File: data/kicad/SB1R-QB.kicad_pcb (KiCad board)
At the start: 4 copper layers, 230 x 228 mm, 5 parts

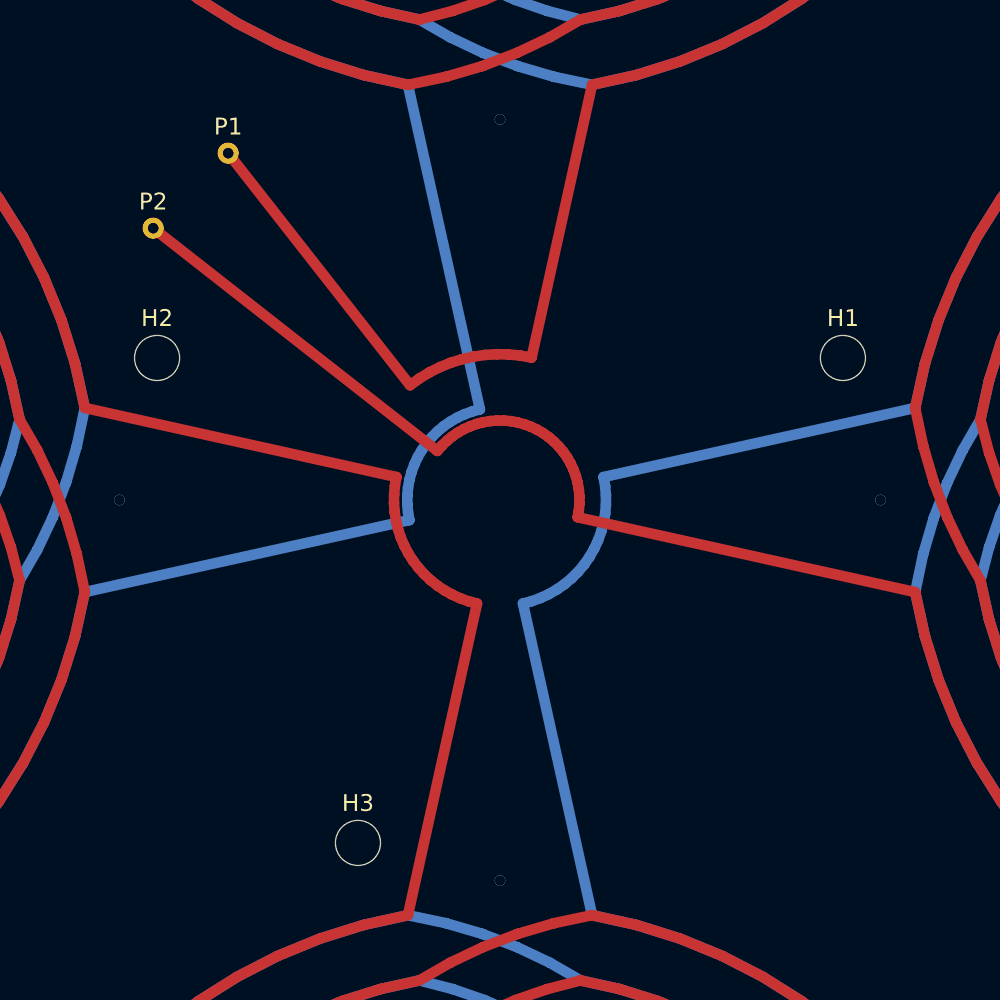
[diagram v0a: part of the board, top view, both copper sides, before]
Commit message: Damping resistors 680 ohm, results, docs and regression for SB1R-Q
- RD1/RD2 value 680 ohm (minimax first gate over Cself 50-200 pF with the
  real AB1T input): 5.1-5.5 us aligned, 7.1-7.5 us at the worst real leak
  (10 mV); gated noise +4 % at 6 us, < 2 % from 20 us. Firmware rule: keep
  BLANK open through turn-off unless the leak exceeds amplifier headroom.
- QB leak after moving its terminals to r23 and re-tuning B (9/9/9/20/6):
  0.07 / 0.59 / 6.0 / 10.3 mV (was 0.005 / 0.85 / 4.4 / 11.0 mV).
- Regenerated SB1R-QA/QB Gerbers and KiCad files, seeds and results;
  sbq_damping.json replaced by sbq_damping2.json; figures SBQ_DAMPING2,
  RX_PLATFORM_QUAD and LEVELS_SCHEMATIC redrawn.
- DESIGN_STATE, CORRECTIONS (5 rows), ASSUMPTIONS (row 14, new row 21),
  OPEN_ITEMS (1 and 12), check counts, stale P01/P02/C04 prompts.
- regress.py: 47 geometry checks, damping fitted, first gate and noise.

Co-Authored-By: Claude Opus 5.5 <noreply@anthropic.com>
Claude-Session: https://claude.ai/code/session_01SK9nuqTzvCJwnmscD6XRZs
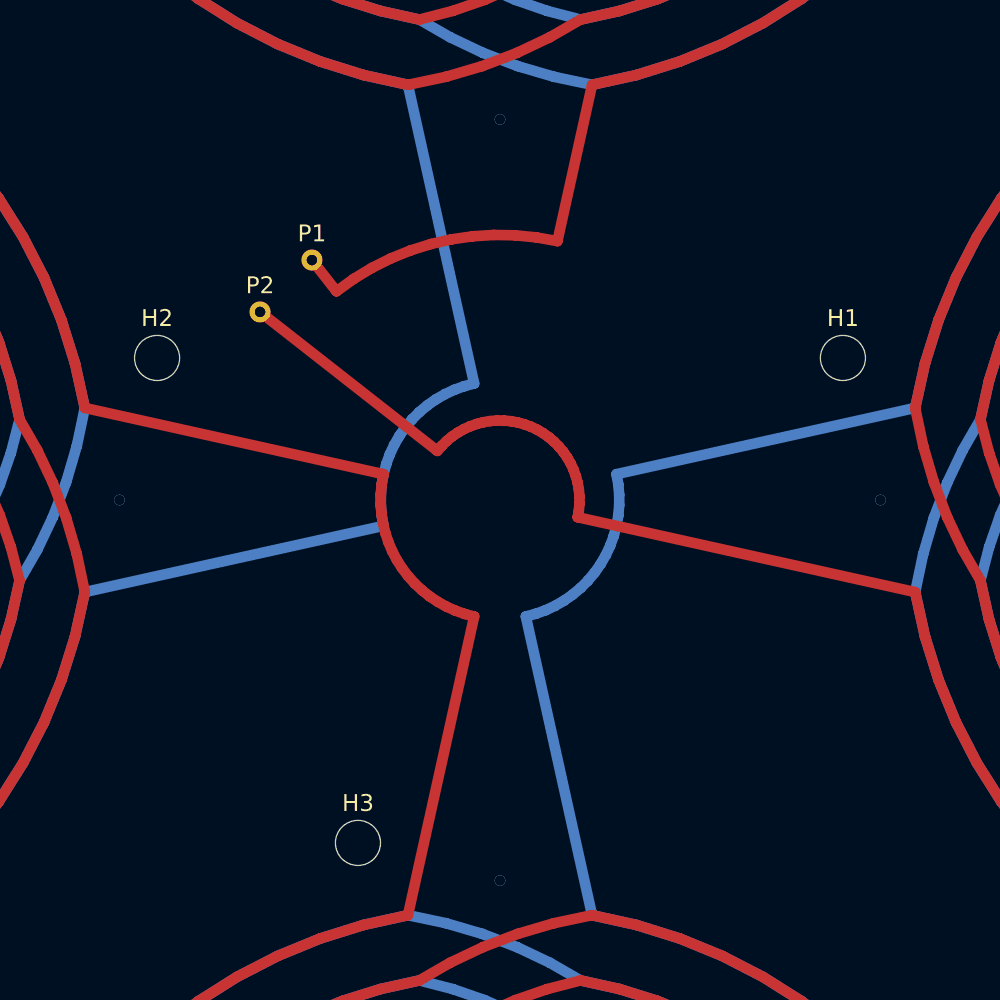
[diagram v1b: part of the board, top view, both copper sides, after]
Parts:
- moved P1 10.2 mm to (135.8, 101.9)
- moved P2 10.2 mm to (131.9, 105.8)
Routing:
- net QB_COIL: track 16992.2 -> 16960.0 mm

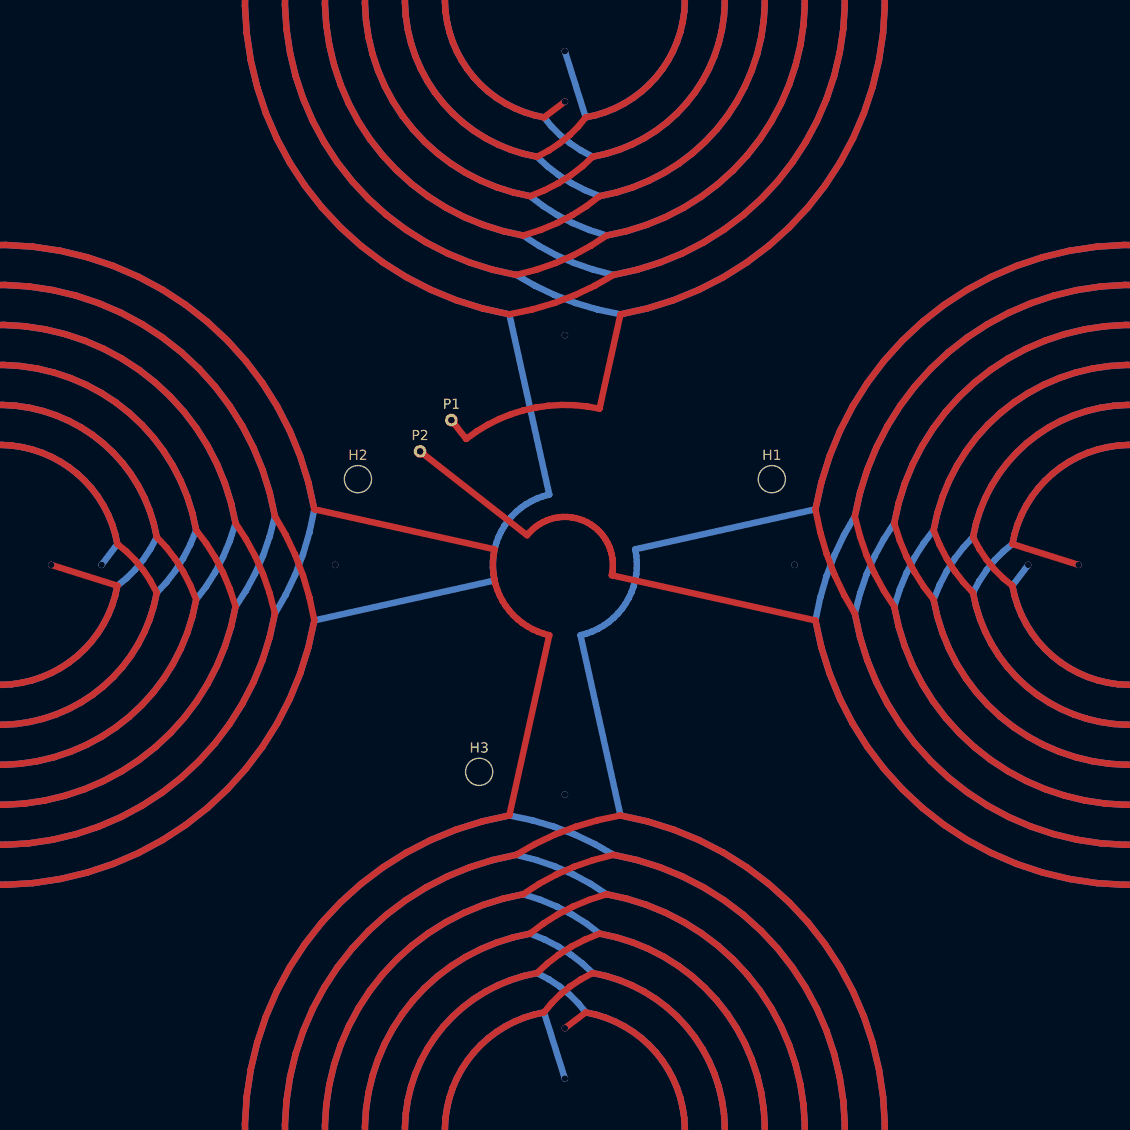
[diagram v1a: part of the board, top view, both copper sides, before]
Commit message: Step 2: CB1D options, SB1R via drill, TXJ1 pads, fab-floor rules, finishes (KiCad 9: 5 boards, 0 errors / 0 unconnected)
- SB1R: via drill 0.4 mm (was 0.8 = no annular ring in the KiCad files and the PTH drill files); QB transfer nets QB_T1/QB_T2; Gerbers SB1R_QA_v2 / SB1R_QB_v2, old marked superseded; sbq sims unchanged (0 numbers moved)
- TXJ1: AWG12 pads 3.8 mm (edge distance 0.6 mm); Gerbers TXJ1_v2
- CB1D: RJB10 0R fitted on JB.10, RJ5/RJ6 DNP grounds for JTR.5/.6 (61 parts, 44/44 nets); Gerbers CB1D_B2; wiring alias JB10_VCM
- dru_gen: conservative Advanced Circuits / TTM floor (UNVERIFIED), SB1R keys; no ENIG near the coil/receivers (immersion silver / HASL); docs/design/FAB_RULES.md
- make kicad-drc covers CB1D, LB1, TXJ1, SB1R-QA/QB; regress 42 pass; CORRECTIONS, DESIGN_STATE, OPEN_ITEMS 23/25-27, ASSUMPTIONS 31

Co-Authored-By: Claude Sonnet 5.5 <noreply@anthropic.com>
Claude-Session: https://claude.ai/code/session_01T7iU5pGiBfkKRBbe2JcTJx
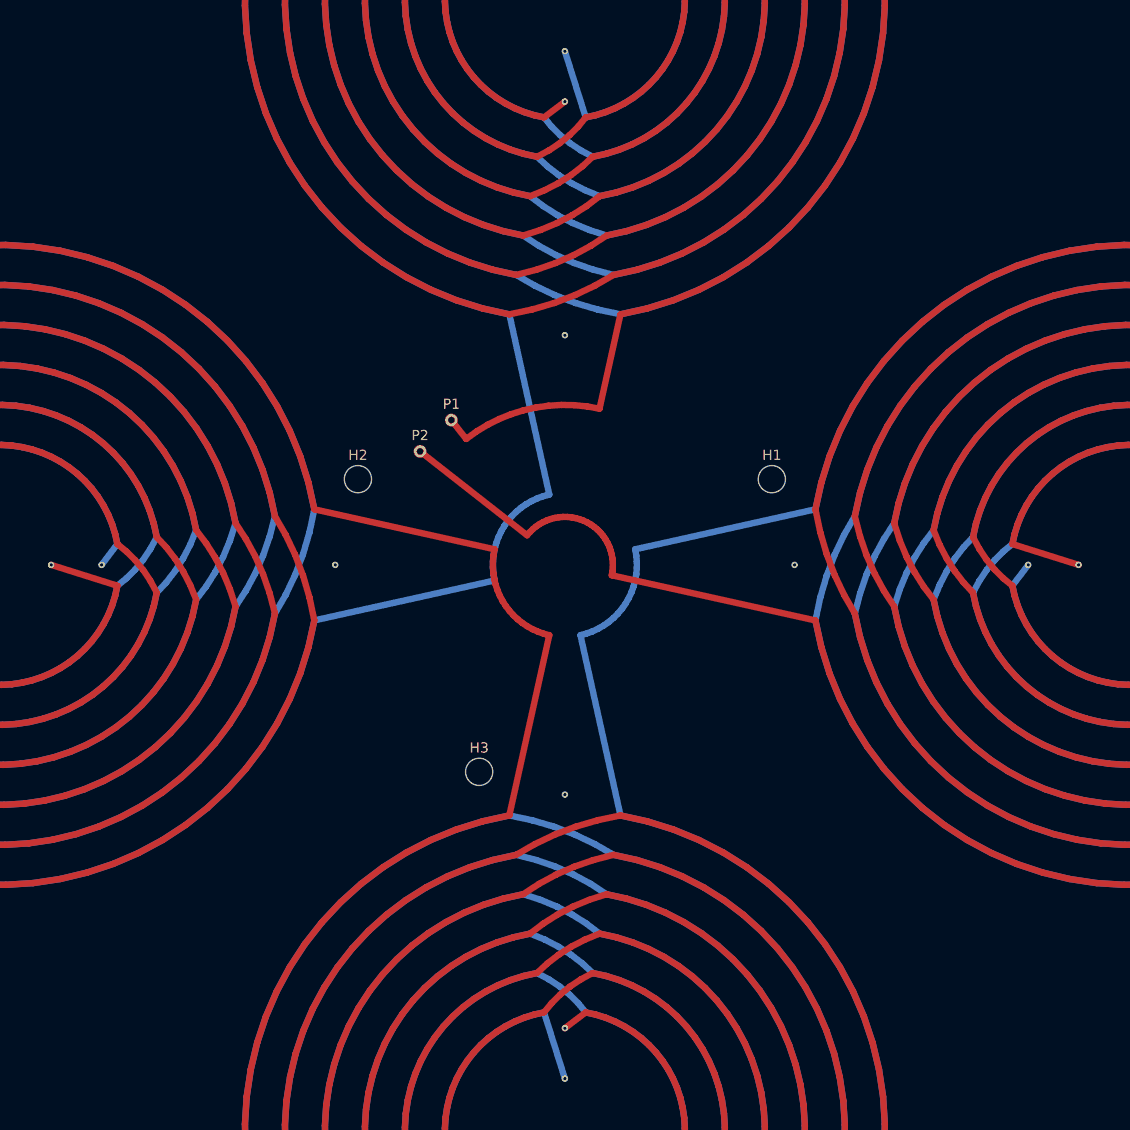
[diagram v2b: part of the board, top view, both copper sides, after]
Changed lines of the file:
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@@
   (paper "A3")
   (layers (0 "F.Cu" signal) (1 "In1.Cu" signal) (2 "In2.Cu" signal) (31 "B.Cu" signal) (34 "B.Paste" user) (35 "F.Paste" user) (36 "B.SilkS" user "B.Silkscreen") (37 "F.SilkS" user "F.Silkscreen") (38 "B.Mask" user) (39 "F.Mask" user) (40 "Dwgs.User" user "User.Drawings") (41 "Cmts.User" user "User.Comments") (44 "Edge.Cuts" user) (47 "F.CrtYd" user "F.Courtyard") (49 "F.Fab" user))
-  (setup (pad_to_mask_clearance 0.05) (stackup (layer "F.Cu" (type "copper") (thickness 0.035)) (layer "dielectric 1" (type "prepreg") (thickness 0.15)) (layer "In1.Cu" (type "copper") (thickness 0.035)) (layer "dielectric 2" (type "core") (thickness 0.34)) (layer "In2.Cu" (type "copper") (thickness 0.035)) (layer "dielectric 3" (type "prepreg") (thickness 0.15)) (layer "B.Cu" (type "copper") (thickness 0.035)) (copper_finish "ENIG")))
+  (setup (pad_to_mask_clearance 0.05) (stackup (layer "F.Cu" (type "copper") (thickness 0.035)) (layer "dielectric 1" (type "prepreg") (thickness 0.15)) (layer "In1.Cu" (type "copper") (thickness 0.035)) (layer "dielectric 2" (type "core") (thickness 0.34)) (layer "In2.Cu" (type "copper") (thickness 0.035)) (layer "dielectric 3" (type "prepreg") (thickness 0.15)) (layer "B.Cu" (type "copper") (thickness 0.035)) (copper_finish "Immersion silver")))
   (net 0 "")
   (net 1 "QB_COIL")
@@
   (segment (start 158.9229 118.8245) (end 158.7865 118.0513) (width 0.8) (layer "B.Cu") (net 1))
   (segment (start 158.7865 118.0513) (end 181.3184 113.0541) (width 0.8) (layer "B.Cu") (net 1))
-  (via (at 150.0000 62.0893) (size 0.8) (drill 0.8) (layers "F.Cu" "B.Cu") (net 1))
-  (via (at 150.0000 91.2893) (size 0.8) (drill 0.8) (layers "F.Cu" "B.Cu") (net 1))
-  (via (at 150.0000 55.7893) (size 0.8) (drill 0.8) (layers "F.Cu" "B.Cu") (net 1))
-  (via (at 92.0893 120.0000) (size 0.8) (drill 0.8) (layers "F.Cu" "B.Cu") (net 1))
-  (via (at 121.2893 120.0000) (size 0.8) (drill 0.8) (layers "F.Cu" "B.Cu") (net 1))
-  (via (at 85.7893 120.0000) (size 0.8) (drill 0.8) (layers "F.Cu" "B.Cu") (net 1))
-  (via (at 150.0000 177.9107) (size 0.8) (drill 0.8) (layers "F.Cu" "B.Cu") (net 1))
-  (via (at 150.0000 148.7107) (size 0.8) (drill 0.8) (layers "F.Cu" "B.Cu") (net 1))
-  (via (at 150.0000 184.2107) (size 0.8) (drill 0.8) (layers "F.Cu" "B.Cu") (net 1))
-  (via (at 207.9107 120.0000) (size 0.8) (drill 0.8) (layers "F.Cu" "B.Cu") (net 1))
-  (via (at 178.7107 120.0000) (size 0.8) (drill 0.8) (layers "F.Cu" "B.Cu") (net 1))
-  (via (at 214.2107 120.0000) (size 0.8) (drill 0.8) (layers "F.Cu" "B.Cu") (net 1))
+  (via (at 150.0000 62.0893) (size 0.8) (drill 0.4) (layers "F.Cu" "B.Cu") (net 1))
+  (via (at 150.0000 91.2893) (size 0.8) (drill 0.4) (layers "F.Cu" "B.Cu") (net 1))
+  (via (at 150.0000 55.7893) (size 0.8) (drill 0.4) (layers "F.Cu" "B.Cu") (net 1))
+  (via (at 92.0893 120.0000) (size 0.8) (drill 0.4) (layers "F.Cu" "B.Cu") (net 1))
+  (via (at 121.2893 120.0000) (size 0.8) (drill 0.4) (layers "F.Cu" "B.Cu") (net 1))
+  (via (at 85.7893 120.0000) (size 0.8) (drill 0.4) (layers "F.Cu" "B.Cu") (net 1))
+  (via (at 150.0000 177.9107) (size 0.8) (drill 0.4) (layers "F.Cu" "B.Cu") (net 1))
+  (via (at 150.0000 148.7107) (size 0.8) (drill 0.4) (layers "F.Cu" "B.Cu") (net 1))
+  (via (at 150.0000 184.2107) (size 0.8) (drill 0.4) (layers "F.Cu" "B.Cu") (net 1))
+  (via (at 207.9107 120.0000) (size 0.8) (drill 0.4) (layers "F.Cu" "B.Cu") (net 1))
+  (via (at 178.7107 120.0000) (size 0.8) (drill 0.4) (layers "F.Cu" "B.Cu") (net 1))
+  (via (at 214.2107 120.0000) (size 0.8) (drill 0.4) (layers "F.Cu" "B.Cu") (net 1))
   (gr_line (start 263.982 118.000) (end 263.930 116.017) (stroke (width 0.1) (type default)) (layer "Edge.Cuts"))
   (gr_line (start 263.930 116.017) (end 263.844 114.034) (stroke (width 0.1) (type default)) (layer "Edge.Cuts"))
